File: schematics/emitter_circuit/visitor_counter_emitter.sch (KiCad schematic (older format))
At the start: 7 parts, among them U1 L7805CV

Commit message: Correction schematics
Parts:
- removed C2: 10uf, symbol Device:CP1
- removed U1: L7805CV, symbol Regulator_Linear:L7805
- added C6: 0,01uF, symbol Device:C_Small
- added C7: 1nF, symbol Device:C_Small
- added R23: 1k, symbol Device:R_Small_US
- added R24: 20k, symbol Device:R_Small_US
- added U6: TLC555IP, Package_DIP:DIP-8_W7.62mm, symbol Timer:TLC555xP
- D4: renamed from D1; value TSHF5410 -> TSHG8200
- R25: renamed from R1; value 33 -> 470
- renumbered C1 to C5, D1 to D3
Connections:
- net at BT?.2 (-), C5.2, D4.1 (K): now also C6.2, C7.2, U6.1 (GND)
- net at R25.1: now also U6.3 (Q)
- net at C5.1, D3.1 (K): now also R23.1, U6.4 (R), U6.8 (VCC)
- new net: C7.1, R24.2, U6.2 (TR), U6.6 (THR)
- new net: C6.1, U6.5 (CV)
- new net: R23.2, R24.1, U6.7 (DIS)
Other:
- moved on the sheet: C5, D3, D4, R25
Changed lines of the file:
@@
 encoding utf-8
 Sheet 1 1
-Title "Visitor counter emiiter"
-Date "2021-02-04"
-Rev "2"
-Comp ""
-Comment1 ""
+Title "Visitor Counter Emitter"
+Date "28-04-2021"
+Rev "3"
+Comp "INFO-2055: Embedded Systems Project"
+Comment1 "Academic Year: 2020-2021"
 Comment2 "JORIS Olivier"
 Comment3 "GOFFART Maxime"
@@
 $EndDescr
 $Comp
-L LED:IR204A D1
+L LED:IR204A D4
 U 1 1 5FE36120
-P 10350 5800
-F 0 "D1" V 10346 5720 50  0000 R CNN
-F 1 "TSHF5410" V 10255 5720 50  0000 R CNN
-F 2 "LED_THT:LED_D3.0mm_IRBlack" H 10350 5975 50  0001 C CNN
-F 3 "http://www.everlight.com/file/ProductFile/IR204-A.pdf" H 10300 5800 50  0001 C CNN
-	1    10350 5800
+P 10450 5450
+F 0 "D4" V 10446 5370 50  0000 R CNN
+F 1 "TSHG8200" V 10355 5370 50  0000 R CNN
+F 2 "LED_THT:LED_D3.0mm_IRBlack" H 10450 5625 50  0001 C CNN
+F 3 "http://www.everlight.com/file/ProductFile/IR204-A.pdf" H 10400 5450 50  0001 C CNN
+	1    10450 5450
 	0    -1   -1   0
 $EndComp
 $Comp
-L Device:R_Small_US R1
+L Device:R_Small_US R25
 U 1 1 5FE36126
-P 10250 5650
-F 0 "R1" H 10250 5855 50  0000 C CNN
-F 1 "33" H 10250 5764 50  0000 C CNN
-F 2 "" V 10250 5650 50  0001 C CNN
-F 3 "~" V 10250 5650 50  0001 C CNN
-	1    10250 5650
+P 10350 5200
+F 0 "R25" H 10350 5405 50  0000 C CNN
+F 1 "470" H 10350 5314 50  0000 C CNN
+F 2 "" V 10350 5200 50  0001 C CNN
+F 3 "~" V 10350 5200 50  0001 C CNN
+	1    10350 5200
 	1    0    0    -1
 $EndComp
-Wire Wire Line
-	9800 5950 9800 6100
 $Comp
-L Diode:1N4149 D1
+L Diode:1N4149 D3
 U 1 1 601D54C1
-P 8400 5650
-F 0 "D1" H 8400 5867 50  0000 C CNN
-F 1 "1N4149" H 8400 5776 50  0000 C CNN
-F 2 "Diode_THT:D_DO-35_SOD27_P7.62mm_Horizontal" H 8400 5475 50  0001 C CNN
-F 3 "http://www.microsemi.com/document-portal/doc_view/11580-lds-0239" H 8400 5650 50  0001 C CNN
-	1    8400 5650
+P 7500 4700
+F 0 "D3" H 7500 4917 50  0000 C CNN
+F 1 "1N4149" H 7500 4826 50  0000 C CNN
+F 2 "Diode_THT:D_DO-35_SOD27_P7.62mm_Horizontal" H 7500 4525 50  0001 C CNN
+F 3 "http://www.microsemi.com/document-portal/doc_view/11580-lds-0239" H 7500 4700 50  0001 C CNN
+	1    7500 4700
 	-1   0    0    -1
 $EndComp
@@
 L Device:Battery_Cell BT?
 U 1 1 601D73F2
-P 8000 5850
-F 0 "BT?" H 8118 5946 50  0001 L CNN
-F 1 "9V" H 8118 5900 50  0000 L CNN
-F 2 "" V 8000 5910 50  0001 C CNN
-F 3 "~" V 8000 5910 50  0001 C CNN
-	1    8000 5850
+P 7350 5050
+F 0 "BT?" H 7468 5146 50  0001 L CNN
+F 1 "9V" H 7468 5100 50  0000 L CNN
+F 2 "" V 7350 5110 50  0001 C CNN
+F 3 "~" V 7350 5110 50  0001 C CNN
+	1    7350 5050
 	1    0    0    -1
 $EndComp
 Wire Wire Line
-	8000 5650 8250 5650
-Wire Wire Line
-	8550 5650 8750 5650
+	7650 4700 7850 4700
 $Comp
-L Device:CP1 C1
+L Device:CP1 C5
 U 1 1 601DA594
-P 8750 5800
-F 0 "C1" H 8865 5846 50  0000 L CNN
-F 1 "100uf" H 8865 5755 50  0000 L CNN
-F 2 "" H 8750 5800 50  0001 C CNN
-F 3 "~" H 8750 5800 50  0001 C CNN
-	1    8750 5800
-	1    0    0    -1
-$EndComp
-Connection ~ 8750 5650
-Wire Wire Line
-	8750 5650 9050 5650
-Wire Wire Line
-	9800 6100 9350 6100
-Wire Wire Line
-	8000 6100 8000 5950
-Connection ~ 9800 6100
-Wire Wire Line
-	8750 5950 8750 6100
-Connection ~ 8750 6100
-Wire Wire Line
-	8750 6100 8000 6100
-Wire Wire Line
-	9350 5950 9350 6100
-Connection ~ 9350 6100
-Wire Wire Line
-	9350 6100 8750 6100
-$Comp
-L Regulator_Linear:L7805 U1
-U 1 1 601D4E99
-P 9350 5650
-F 0 "U1" H 9350 5892 50  0000 C CNN
-F 1 "L7805CV" H 9350 5801 50  0000 C CNN
-F 2 "" H 9375 5500 50  0001 L CIN
-F 3 "http://www.st.com/content/ccc/resource/technical/document/datasheet/41/4f/b3/b0/12/d4/47/88/CD00000444.pdf/files/CD00000444.pdf/jcr:content/translations/en.CD00000444.pdf" H 9350 5600 50  0001 C CNN
-	1    9350 5650
+P 7850 4850
+F 0 "C5" H 7965 4896 50  0000 L CNN
+F 1 "100uf" H 7965 4805 50  0000 L CNN
+F 2 "" H 7850 4850 50  0001 C CNN
+F 3 "~" H 7850 4850 50  0001 C CNN
+	1    7850 4850
 	1    0    0    -1
 $EndComp
 Wire Wire Line
-	10350 5650 10350 5700
+	8850 5600 8700 5600
 Wire Wire Line
-	10350 6000 10350 6100
-Wire Wire Line
-	10350 6100 9800 6100
-Wire Wire Line
-	9650 5650 10150 5650
+	10450 5200 10450 5350
 $Comp
-L Device:CP1 C2
-U 1 1 602A9A75
-P 9800 5800
-F 0 "C2" H 9915 5846 50  0000 L CNN
-F 1 "10uf" H 9915 5755 50  0000 L CNN
-F 2 "" H 9800 5800 50  0001 C CNN
-F 3 "~" H 9800 5800 50  0001 C CNN
-	1    9800 5800
+L Device:R_Small_US R23
+U 1 1 608A2E48
+P 9750 4700
+F 0 "R23" H 9750 4905 50  0000 C CNN
+F 1 "1k" H 9750 4814 50  0000 C CNN
+F 2 "" V 9750 4700 50  0001 C CNN
+F 3 "~" V 9750 4700 50  0001 C CNN
+	1    9750 4700
 	1    0    0    -1
 $EndComp
+Wire Wire Line
+	7350 4700 7350 4850
+Wire Wire Line
+	8700 4700 9350 4700
+Wire Wire Line
+	9650 4700 9350 4700
+Connection ~ 9350 4700
+Wire Wire Line
+	9850 4700 9950 4700
+Wire Wire Line
+	9950 5400 9850 5400
+Connection ~ 9950 5400
+$Comp
+L Device:R_Small_US R24
+U 1 1 608A8837
+P 9950 5500
+F 0 "R24" H 9950 5705 50  0000 C CNN
+F 1 "20k" H 9950 5614 50  0000 C CNN
+F 2 "" V 9950 5500 50  0001 C CNN
+F 3 "~" V 9950 5500 50  0001 C CNN
+	1    9950 5500
+	0    1    1    0
+$EndComp
+Wire Wire Line
+	9850 5600 9950 5600
+Wire Wire Line
+	9850 5200 10250 5200
+Wire Wire Line
+	8700 4700 8700 5600
+Wire Wire Line
+	9350 4700 9350 5000
+Wire Wire Line
+	9950 4700 9950 5400
+Connection ~ 7850 4700
+Wire Wire Line
+	7850 4700 8700 4700
+Connection ~ 8700 4700
+$Comp
+L Timer:TLC555xP U6
+U 1 1 60896685
+P 9350 5400
+F 0 "U6" H 9350 5981 50  0000 C CNN
+F 1 "TLC555IP" H 9350 5890 50  0000 C CNN
+F 2 "Package_DIP:DIP-8_W7.62mm" H 10000 5000 50  0001 C CNN
+F 3 "http://www.ti.com/lit/ds/symlink/tlc555.pdf" H 10200 5000 50  0001 C CNN
+	1    9350 5400
+	1    0    0    -1
+$EndComp
+$Comp
+L Device:C_Small C7
+U 1 1 608BCDBE
+P 8600 6100
+F 0 "C7" H 8692 6146 50  0000 L CNN
+F 1 "1nF" H 8692 6055 50  0000 L CNN
+F 2 "" H 8600 6100 50  0001 C CNN
+F 3 "~" H 8600 6100 50  0001 C CNN
+	1    8600 6100
+	1    0    0    -1
+$EndComp
+$Comp
+L Device:C_Small C6
+U 1 1 608B0E3A
+P 8150 6100
+F 0 "C6" H 8242 6146 50  0000 L CNN
+F 1 "0,01uF" H 8242 6055 50  0000 L CNN
+F 2 "" H 8150 6100 50  0001 C CNN
+F 3 "~" H 8150 6100 50  0001 C CNN
+	1    8150 6100
+	1    0    0    -1
+$EndComp
+Wire Wire Line
+	9950 5600 9950 5900
+Connection ~ 9950 5600
+Wire Wire Line
+	7850 5000 7850 6250
+Wire Wire Line
+	7350 5150 7350 6250
+Wire Wire Line
+	9350 5800 9350 6250
+Wire Wire Line
+	10450 6250 9350 6250
+Wire Wire Line
+	10450 5650 10450 6250
+Connection ~ 7850 6250
+Wire Wire Line
+	7850 6250 7350 6250
+Connection ~ 9350 6250
+Wire Wire Line
+	8850 5200 8600 5200
+Wire Wire Line
+	8600 5200 8600 5900
+Wire Wire Line
+	9950 5900 8600 5900
+Connection ~ 8600 5900
+Wire Wire Line
+	8600 5900 8600 6000
+Wire Wire Line
+	7850 6250 8150 6250
+Wire Wire Line
+	8850 5400 8150 5400
+Wire Wire Line
+	8150 5400 8150 6000
+Wire Wire Line
+	8150 6200 8150 6250
+Connection ~ 8150 6250
+Wire Wire Line
+	8150 6250 8600 6250
+Wire Wire Line
+	8600 6200 8600 6250
+Connection ~ 8600 6250
+Wire Wire Line
+	8600 6250 9350 6250
 $EndSCHEMATC

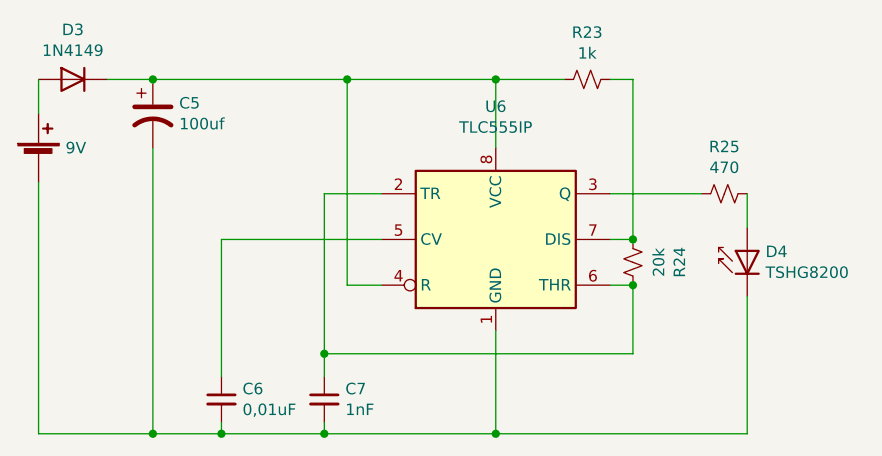
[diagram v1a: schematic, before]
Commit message: Modif schematic emitter
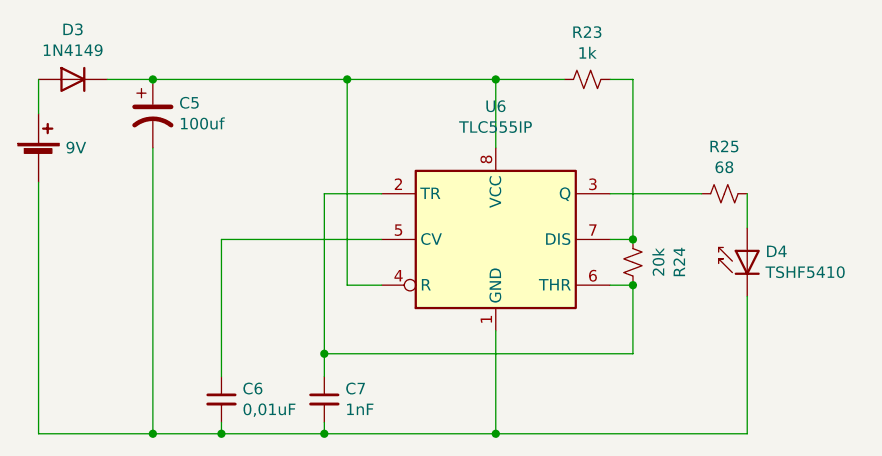
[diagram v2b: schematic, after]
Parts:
- D4: value TSHG8200 -> TSHF5410
- R25: value 470 -> 68
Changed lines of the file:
@@
 P 10450 5450
 F 0 "D4" V 10446 5370 50  0000 R CNN
-F 1 "TSHG8200" V 10355 5370 50  0000 R CNN
+F 1 "TSHF5410" V 10355 5370 50  0000 R CNN
 F 2 "LED_THT:LED_D3.0mm_IRBlack" H 10450 5625 50  0001 C CNN
 F 3 "http://www.everlight.com/file/ProductFile/IR204-A.pdf" H 10400 5450 50  0001 C CNN
@@
 P 10350 5200
 F 0 "R25" H 10350 5405 50  0000 C CNN
-F 1 "470" H 10350 5314 50  0000 C CNN
+F 1 "68" H 10350 5314 50  0000 C CNN
 F 2 "" V 10350 5200 50  0001 C CNN
 F 3 "~" V 10350 5200 50  0001 C CNN
